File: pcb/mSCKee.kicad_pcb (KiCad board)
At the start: 4 copper layers, 275.3 x 124.4 mm, 192 parts, among them IC1 PCA9956BTWY, IC2 PCA9956BTWY, J2 4P4C, J3 4P4C, J4 USB_C_Receptacle_USB2.0_16P, SW1 SW_Push_45deg, SW10 SW_Push_45deg, SW11 SW_Push_45deg, SW12 SW_Push_45deg, SW13 SW_Push_45deg, SW14 SW_Push_45deg, SW15 SW_Push_45deg, SW16 SW_Push_45deg, SW17 SW_Push_45deg, SW18 SW_Push_45deg, SW19 SW_Push_45deg, SW2 SW_Push_45deg, SW20 SW_Push_45deg, SW21 SW_Push_45deg, SW22 SW_Push_45deg, SW23 SW_Push_45deg, SW24 SW_Push_45deg, SW25 SW_Push_45deg, SW26 SW_Push_45deg, SW27 SW_Push_45deg, SW28 SW_Push_45deg, SW29 SW_Push_45deg, SW3 SW_Push_45deg, SW30 SW_Push_45deg, SW31 SW_Push_45deg, SW32 SW_Push_45deg, SW33 SW_Push_45deg, SW34 SW_Push_45deg, SW35 SW_Push_45deg, SW36 SW_Push_45deg, SW4 SW_Push_45deg, SW5 SW_Push_45deg, SW6 SW_Push_45deg, SW7 SW_Push_45deg, SW8 SW_Push_45deg, SW9 SW_Push_45deg, U1 W25Q128JVSIQ, U2 RP2040, U3 NCP1117LPST33T3G, U4 OPT3001DNPR, U5 NCP1117LPST33T3G, U6 MCP23017T-E/ML, U7 OPT3001DNPR, Y1 ABM8-272-T3

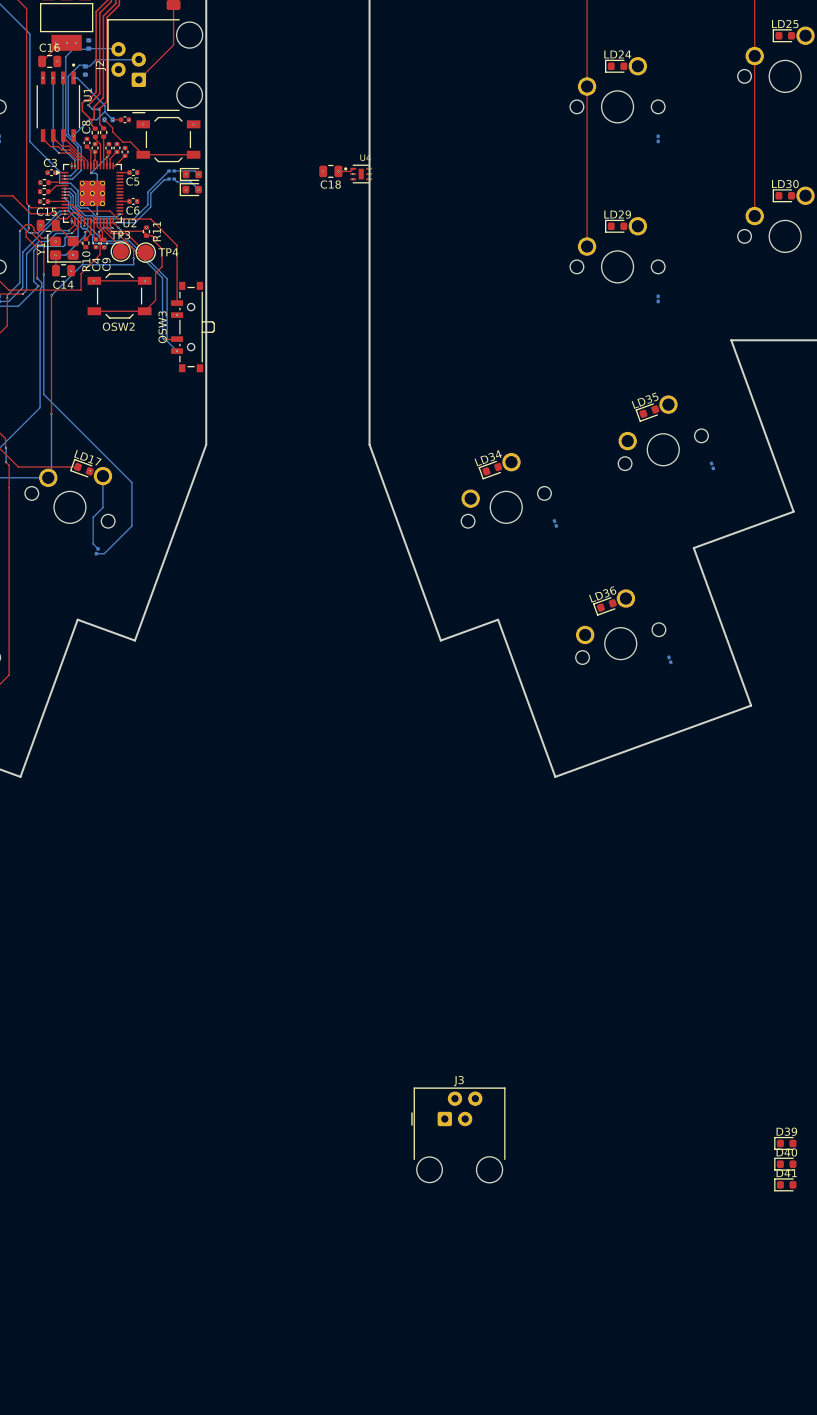
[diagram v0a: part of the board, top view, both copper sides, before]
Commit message: fix: Change MCP23017 ROW pins to _R ones
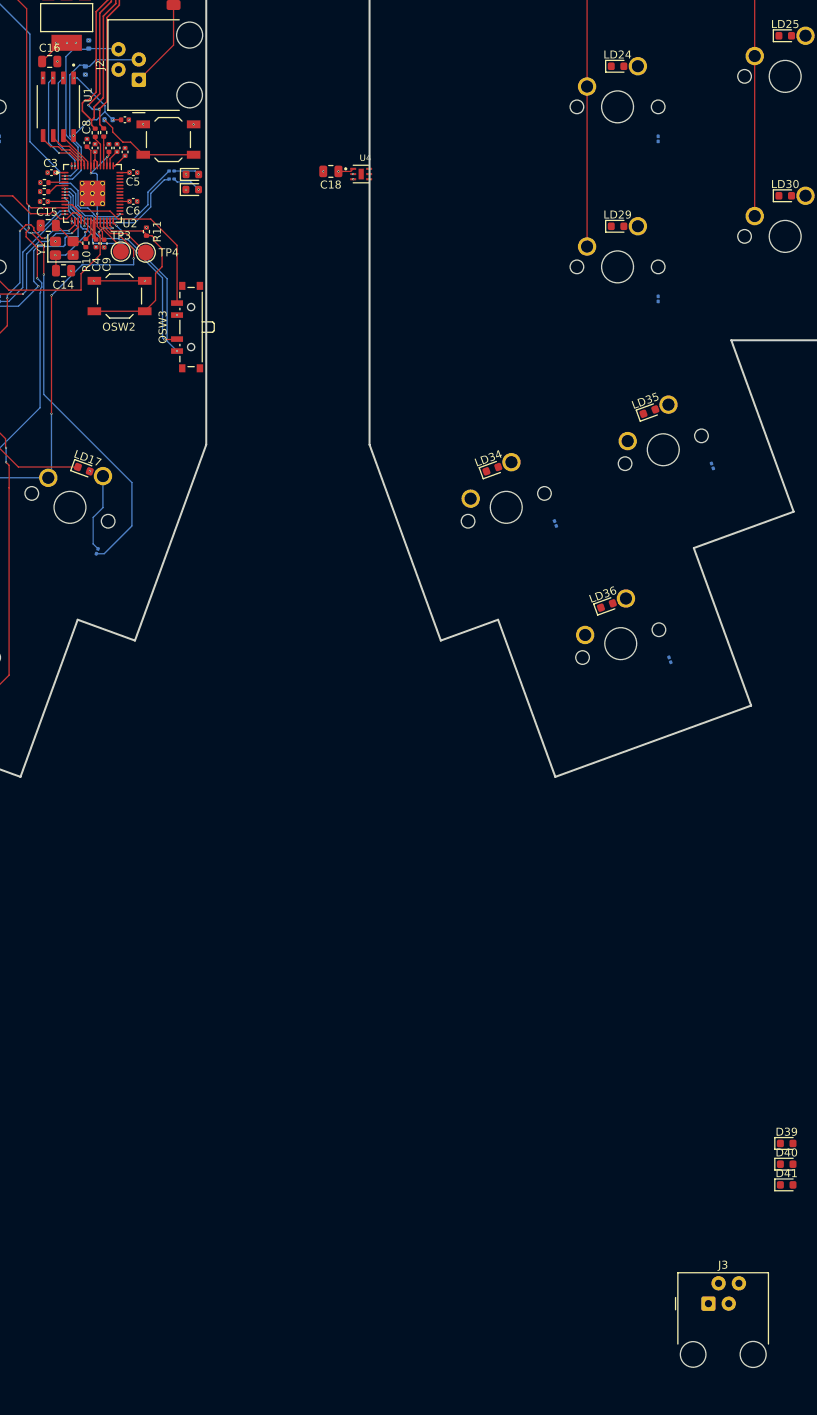
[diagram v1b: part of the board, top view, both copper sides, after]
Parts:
- moved J3 40.2 mm to (261.4, 257.2)
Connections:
- U6 pad 17: ROW2 -> ROW2_R
- U6 pad 18: ROW1 -> ROW1_R
- U6 pad 19: ROW0 -> ROW0_R
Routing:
- net +3V3: vias 22 -> 21

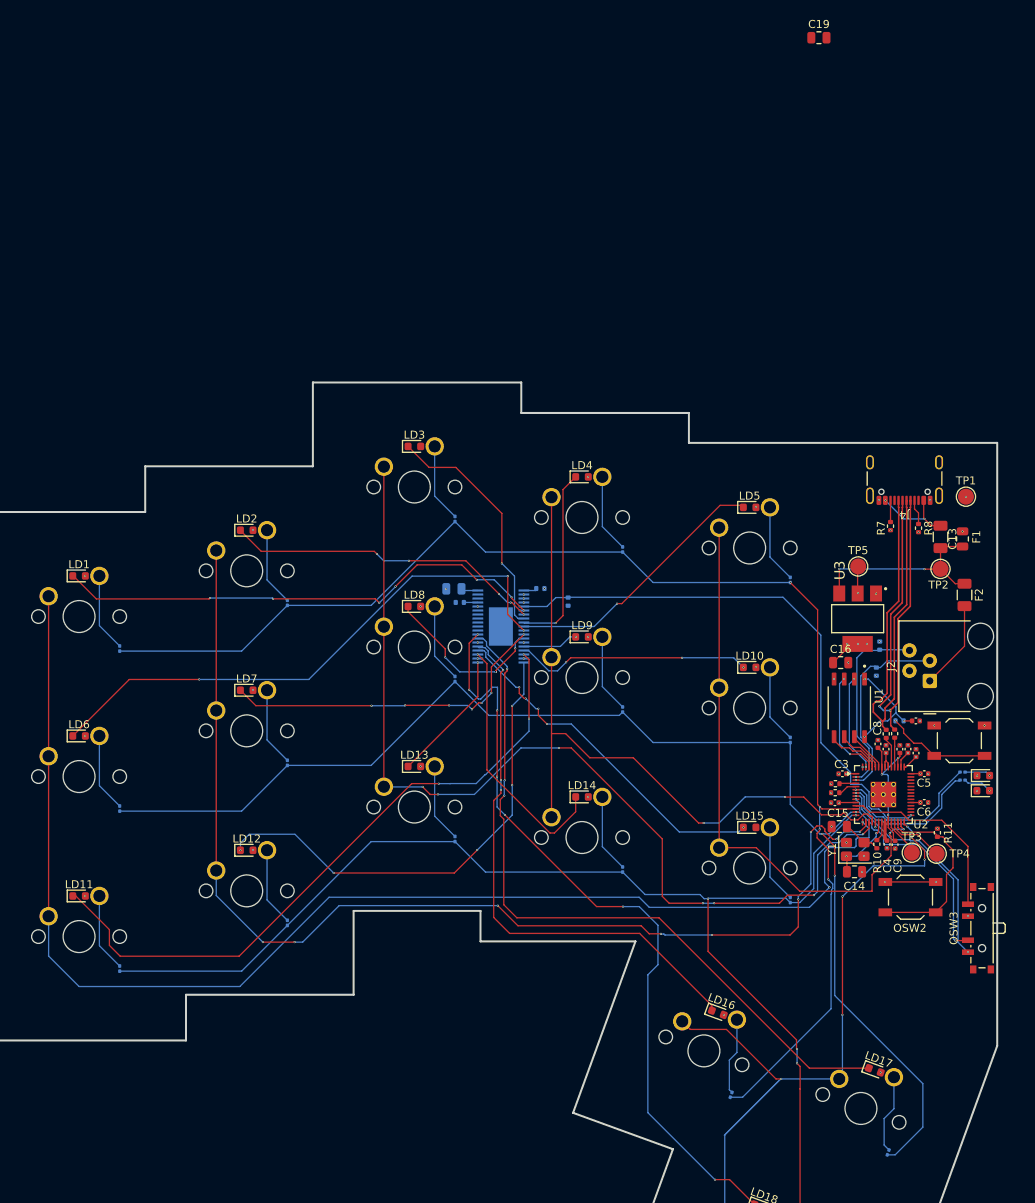
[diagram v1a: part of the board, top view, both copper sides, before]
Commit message: fix(left side): Made power traces wider, simplified W25Q128 storage interrupt switch routing with vias to 3.3V
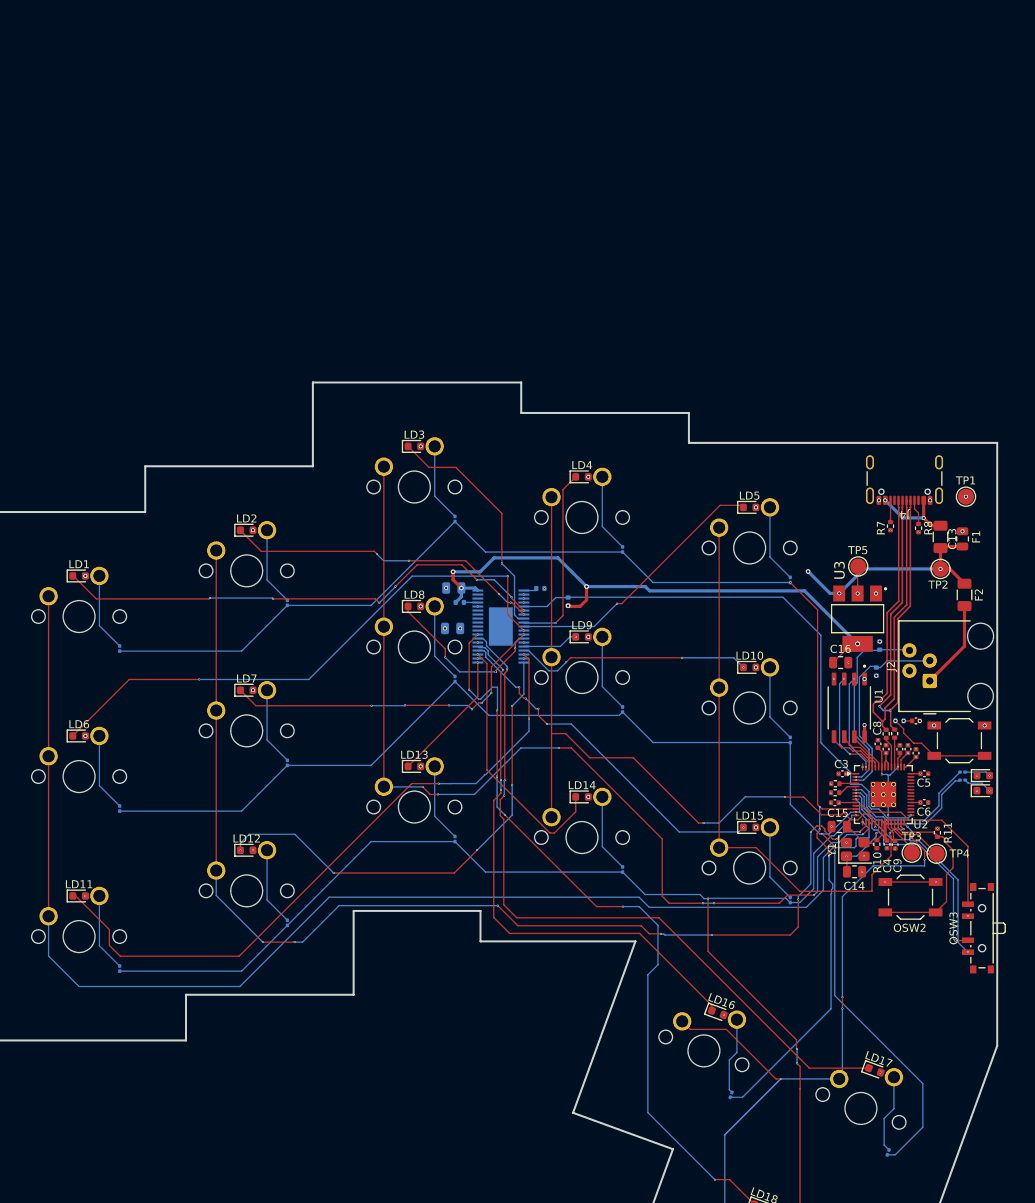
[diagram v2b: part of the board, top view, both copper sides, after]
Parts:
- C19: moved to B.Cu
- moved C19 86.9 mm to (130.5, 97.7), turned to 180 degrees
- moved C17 0.10 mm to (130.7, 92.6)
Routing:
- net +3V3: track 39.3 -> 92.7 mm, vias 21 -> 24
- net +5V: track 25.0 -> 28.2 mm, vias 18 -> 22
- net Net-(U2-VREG_VOUT): track 17.7 -> 16.4 mm
- net COL0: track 164.1 -> 163.1 mm, vias 2 -> 1
- net Net-(F2-Pad2): track 11.1 -> 11.2 mm, vias 1 -> 0
- net GND: vias 51 -> 48
- net (no net): vias 0 -> 4

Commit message: feat: left: Wire up OPT3001 light sensor, wire up rest of I2C bus to PCA9956 LED driver, right side: Wire up ROWs to MCP23017, fix: change right thumb cluster from COL7 to COL6
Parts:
- IC2: moved to B.Cu
- moved U6 158.1 mm to (229.5, 109.2)
- moved IC2 111.7 mm to (281.9, 100.5), turned to 180 degrees
- moved U4 22.5 mm to (196.7, 123.2)
- moved C18 18.3 mm to (196.6, 120.8)
- moved R4 0.36 mm to (183.8, 102.9)
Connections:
- SW34 pad 1: COL7 -> COL6
- SW35 pad 1: COL7 -> COL6
- SW36 pad 1: COL7 -> COL6
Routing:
- net ROW2_R: track 0.00 -> 130.3 mm, vias 0 -> 1
- net ROW0_R: track 0.00 -> 123.5 mm, vias 0 -> 1
- net ROW1_R: track 0.00 -> 118.0 mm, vias 0 -> 1
- net I2C_CLK: track 2.40 -> 117.9 mm, vias 0 -> 17
- net I2C_D: track 2.08 -> 110.0 mm, vias 0 -> 18
- net COL5: track 93.9 -> 90.2 mm
- net +3V3: track 92.7 -> 94.6 mm, vias 24 -> 25
- net COL4: track 72.7 -> 71.5 mm
- net COL2: track 123.9 -> 123.1 mm, vias 7 -> 5
- net (no net): vias 4 -> 0

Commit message: feat(right side): Add same copper pours as left side, route NCP1117 and other power components
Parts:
- R18: moved to B.Cu
- moved F3 190.6 mm to (223.3, 93.3)
- moved U5 184.4 mm to (233.8, 91.6)
- moved J3 160.3 mm to (227.5, 100.5), turned to -90 degrees
- moved C21 160.3 mm to (237.5, 86.9)
- moved C20 155.4 mm to (227.4, 92.5), turned to 90 degrees
- moved TP6 151.7 mm to (233.6, 86.5)
- moved C23 125.7 mm to (234.8, 130.6)
- moved C22 125.7 mm to (234.8, 127.6)
- moved C24 125.7 mm to (234.8, 133.6)
- moved C25 125.7 mm to (234.8, 136.6)
- moved D39 125.7 mm to (222.4, 121.3)
- moved D40 125.7 mm to (222.4, 123.9)
- moved D41 125.7 mm to (222.4, 126.5)
- moved R18 123.2 mm to (284.9, 95.6), turned to 180 degrees
- moved R17 102.9 mm to (224.4, 132.8)
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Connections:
- C20 pad 2: unconnected-(C20-Pad2) -> R_GND
- C21 pad 2: unconnected-(C21-Pad2) -> R_GND
- J3 pad 2: unconnected-(J3-Pad2) -> R_GND
- R18 pad 1: unconnected-(R18-Pad1) -> R_GND
- U5 pad 1: unconnected-(U5-GND-Pad1) -> R_GND
- U6 pad 11: Net-(U6-A0) -> R_GND
- U6 pad 12: Net-(U6-A0) -> R_GND
- U6 pad 13: Net-(U6-A0) -> R_GND
- U6 pad 29: unconnected-(U6-HTAB-Pad29) -> R_GND
- U7 pad 2: unconnected-(U7-ADDR-Pad2) -> R_GND
- U7 pad 3: unconnected-(U7-GND-Pad3) -> R_GND
- U7 pad 7: unconnected-(U7-EXP-Pad7) -> R_GND
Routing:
- net R_GND: track 0.00 -> 13.3 mm, vias 0 -> 6
- net Net-(F3-Pad1): track 0.00 -> 9.59 mm
- net +3V3_R: track 0.00 -> 8.04 mm, vias 0 -> 2
- net +5V_R: track 0.00 -> 6.17 mm, vias 0 -> 1
- net ROW2_R: track 130.3 -> 125.6 mm
- net ROW1: track 160.4 -> 157.4 mm
- net ROW1_R: track 118.0 -> 120.6 mm
- net ROW0_R: track 123.5 -> 126.1 mm
- net GND: track 6.96 -> 8.45 mm
- net Net-(IC2-REXT): track 0.00 -> 1.36 mm
- net I2C_CLK_R: vias 2 -> 1
- added copper zone on In2.Cu, net +3V3_R
- added copper zone on In2.Cu, net +5V_R
- added copper zone on In1.Cu, net R_GND

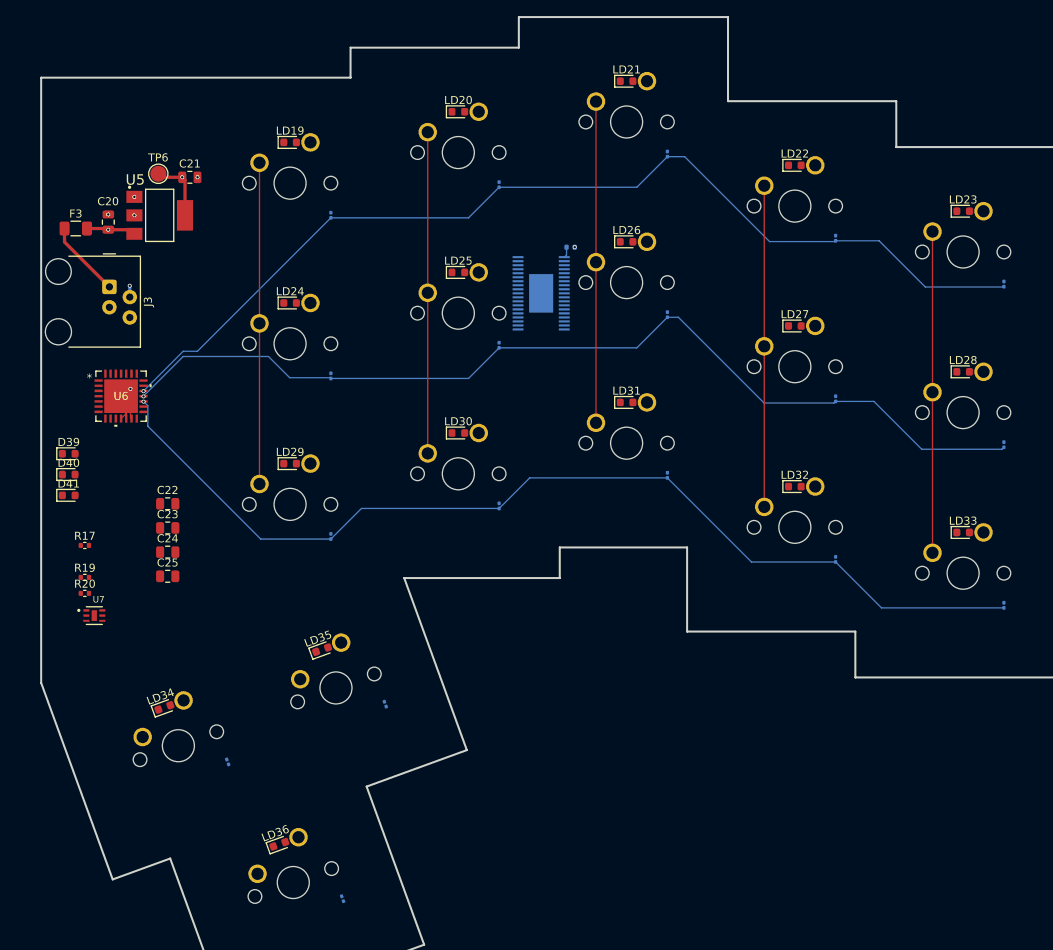
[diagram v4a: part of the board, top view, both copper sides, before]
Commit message: feat: Route entire right half: matrix, LEDs, OPT3001, I2C
Should all be finished, maybe I made some mistakes.
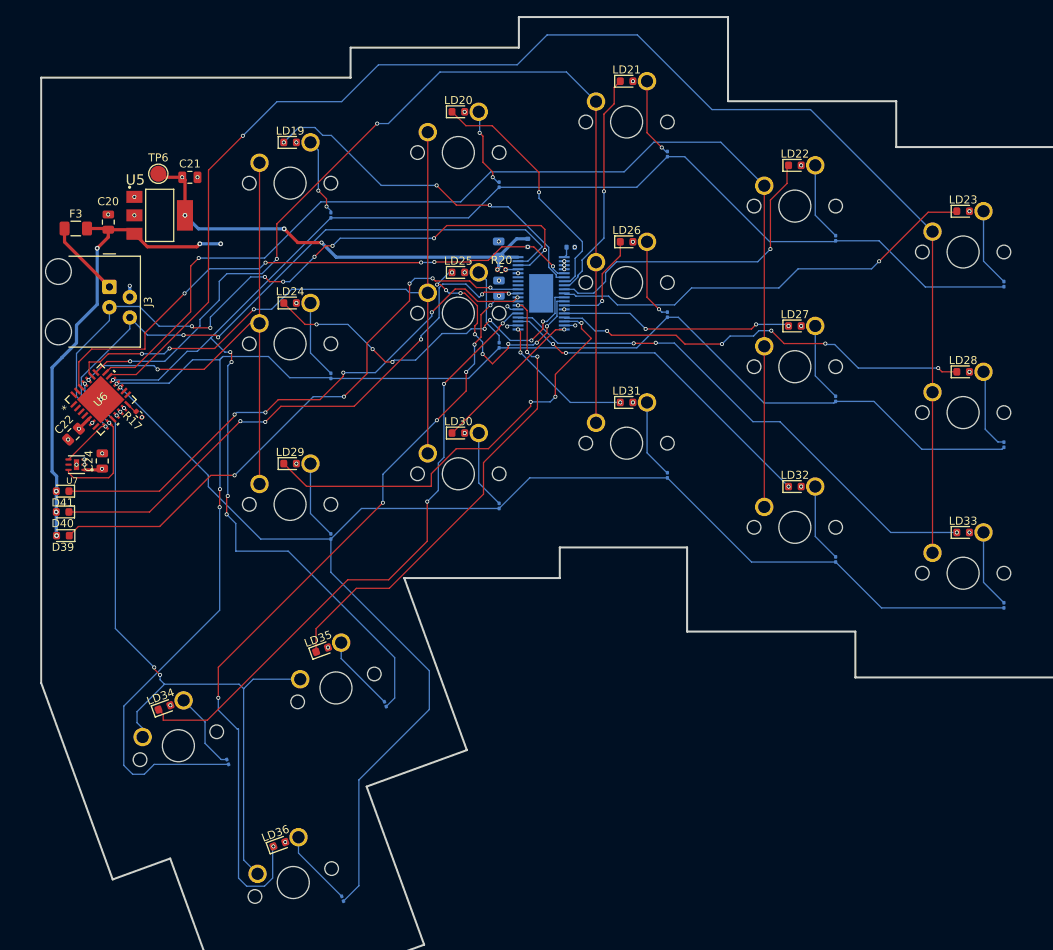
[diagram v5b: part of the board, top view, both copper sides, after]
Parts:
- C23, C25, R19: moved to B.Cu
- moved R19 69.1 mm to (279.6, 95.1), turned to 90 degrees
- moved R20 65.7 mm to (276.3, 98.4)
- moved C25 54.7 mm to (276.0, 100.7), turned to 90 degrees
- moved C23 53.9 mm to (276.0, 95.8), turned to -90 degrees
- moved U7 18.9 mm to (223.4, 122.7), turned to 180 degrees
- moved R17 17.7 mm to (231.2, 116.4), turned to 135 degrees
- moved C22 14.6 mm to (223.0, 118.9), turned to 45 degrees
- moved C24 14.0 mm to (226.6, 122.2), turned to 90 degrees
- moved D39 10.2 mm to (221.7, 131.5), turned to 180 degrees
- moved D40 4.72 mm to (221.7, 128.6), turned to 180 degrees
- moved U6 2.56 mm to (226.4, 114.6), turned to 45 degrees
- moved D41 0.92 mm to (221.7, 126.0), turned to 180 degrees
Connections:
- C22 pad 1: unconnected-(C22-Pad1) -> R_GND
- C23 pad 1: unconnected-(C23-Pad1) -> R_GND
- C24 pad 2: unconnected-(C24-Pad2) -> R_GND
- IC2 pad 14: unconnected-(IC2-VSS-Pad14) -> R_GND
- IC2 pad 18: unconnected-(IC2-VSS-Pad18) -> R_GND
- IC2 pad 2: Net-(IC2-AD0) -> R_GND
- IC2 pad 21: unconnected-(IC2-VSS-Pad21) -> R_GND
- IC2 pad 25: unconnected-(IC2-VSS-Pad25) -> R_GND
- IC2 pad 3: Net-(IC2-AD0) -> R_GND
- IC2 pad 34: unconnected-(IC2-VSS-Pad34) -> R_GND
- IC2 pad 4: Net-(IC2-AD0) -> R_GND
- U6 pad 6: unconnected-(U6-VSS-Pad6) -> R_GND
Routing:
- net COL11: track 40.0 -> 179.9 mm, vias 0 -> 1
- net COL10: track 40.0 -> 139.5 mm, vias 0 -> 1
- net Net-(IC2-LED17): track 0.00 -> 99.2 mm, vias 0 -> 7
- net S_M_CLOCK: track 0.00 -> 93.2 mm, vias 0 -> 9
- net S_M_DATA: track 0.00 -> 92.6 mm, vias 0 -> 3
- net COL6: track 0.00 -> 91.2 mm, vias 0 -> 3
- net COL9: track 40.0 -> 123.9 mm, vias 0 -> 3
- net Net-(IC2-LED15): track 0.00 -> 77.1 mm, vias 0 -> 3
- net Net-(D39-K): track 0.00 -> 73.2 mm, vias 0 -> 5
- net ROW1_R: track 120.6 -> 193.3 mm, vias 1 -> 3
- net OE_ENABLE_R: track 0.00 -> 72.4 mm, vias 0 -> 6
- net Net-(D40-K): track 0.00 -> 71.3 mm, vias 0 -> 5
- net Net-(D41-K): track 0.00 -> 67.9 mm, vias 0 -> 5
- net Net-(IC2-LED14): track 0.00 -> 65.9 mm, vias 0 -> 3
- net ROW0_R: track 126.1 -> 189.9 mm, vias 1 -> 5
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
